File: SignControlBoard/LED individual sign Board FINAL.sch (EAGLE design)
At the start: 25 parts, among them U1 ATMEGA328P, U2 M5205 5v, X1 22-23-2021, Y1 16MHz

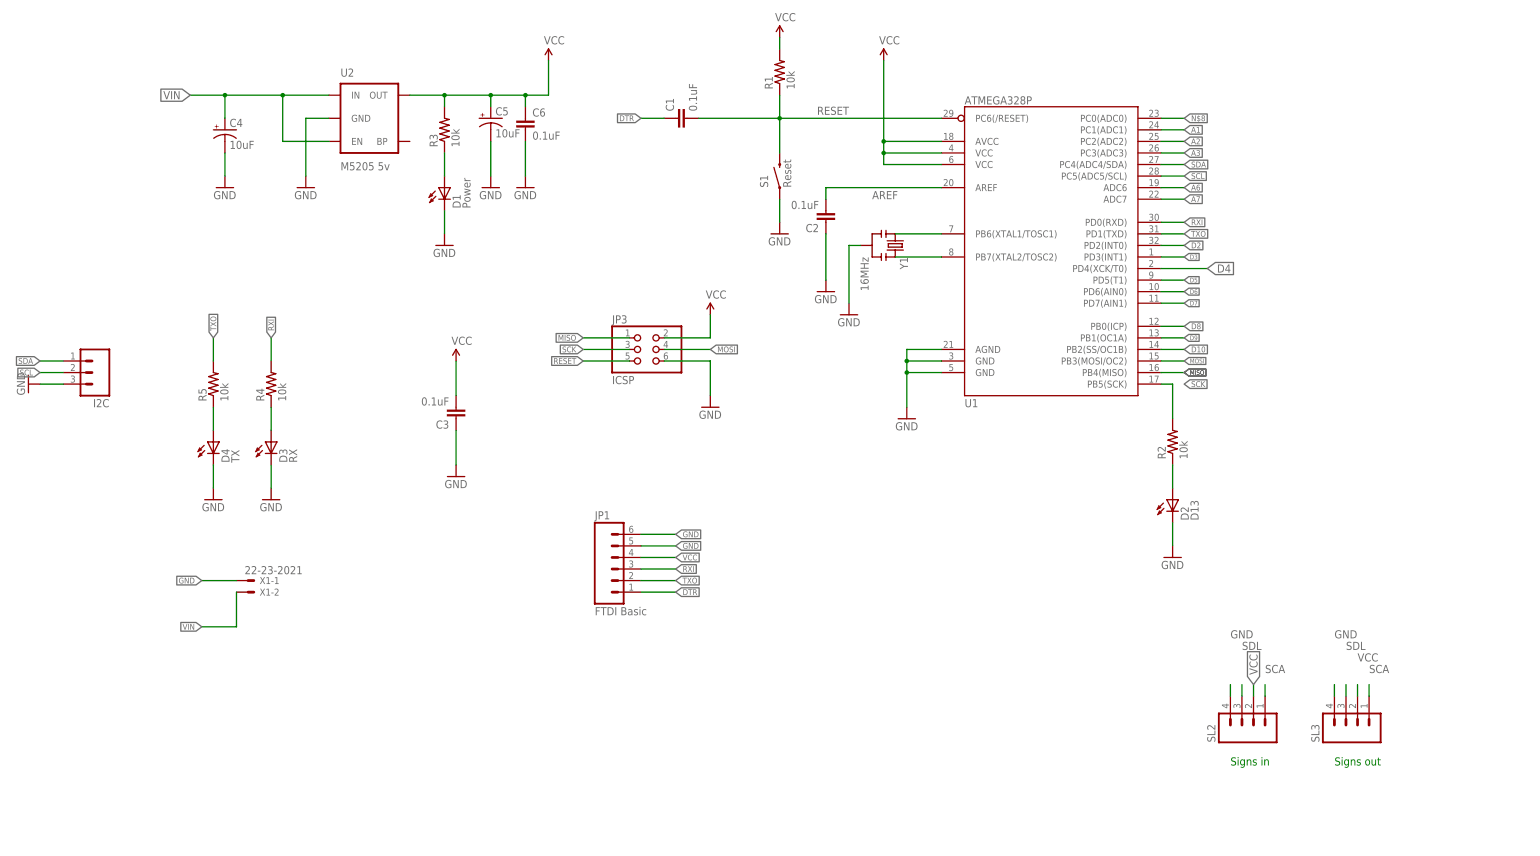
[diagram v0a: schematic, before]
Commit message: Updated control and sign boards. Removed old versions
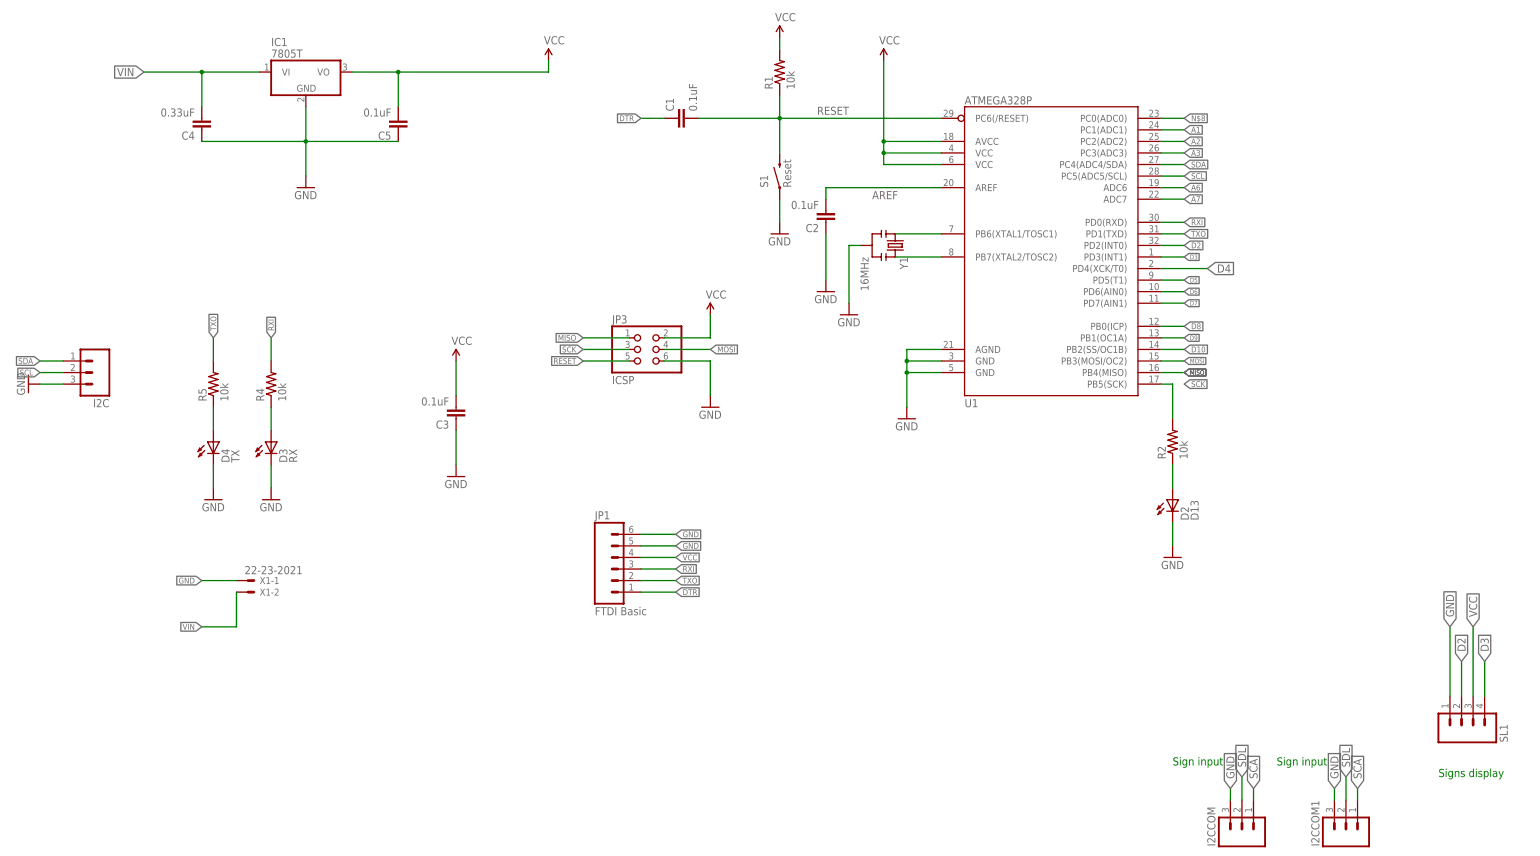
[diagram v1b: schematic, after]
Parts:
- removed C6: 0.1uF, SparkFun-Passives:CAP0603-CAP
- removed D1: Power, SparkFun-LED:LED-RED0603
- removed R3: 10k, SparkFun-Passives:RESISTOR0603-RES
- removed SL2, SL3: (no value), con-amp-quick:M04
- removed U2: M5205 5v, SparkFun-PowerIC:MIC52055V
- added I2CCOM, I2CCOM1: (no value), SparkFun-Connectors:M03PTH
- added IC1: 7805T, linear:7805T
- added SL1: (no value), con-amp-quick:M04
- C4: value 10uF -> 0.33uF; device SparkFun-Passives:CAP_POL1206 -> SparkFun-Passives:CAP0603-CAP
- C5: value 10uF -> 0.1uF; device SparkFun-Passives:CAP_POL1206 -> SparkFun-Passives:CAP0603-CAP
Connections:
- removed net N$3: D1.A, R3.1
- net D2: now also SL1.2
- net D3: now also SL1.4
- net GND: now also C4.1, C5.1, I2CCOM.3, I2CCOM1.3, IC1.GND, SL1.1; no longer C4.-, C5.-, C6.2, D1.C, SL2.4, SL3.4, U2.GND
- net SCA: now also I2CCOM.1, I2CCOM1.1; no longer SL2.1, SL3.1
- net SDL: now also I2CCOM.2, I2CCOM1.2; no longer SL2.3, SL3.3
- net VCC: now also C5.2, IC1.VO, SL1.3; no longer C5.+, C6.1, R3.2, SL2.2, SL3.2, U2.OUT
- net VIN: now also C4.2, IC1.VI; no longer C4.+, U2.EN, U2.IN
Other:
- note added: "Sign input"
- note added: "Signs display"
- note removed: "Signs in"
- note removed: "Signs out"
